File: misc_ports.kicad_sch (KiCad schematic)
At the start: 0 parts

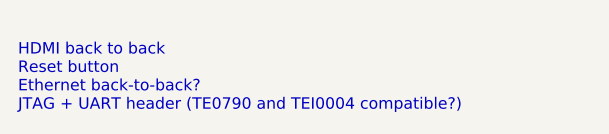
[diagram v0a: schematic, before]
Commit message: add reset button
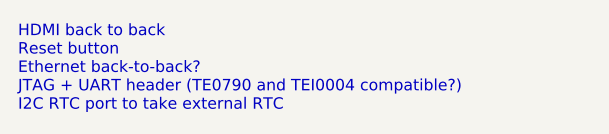
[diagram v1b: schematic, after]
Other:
- note added: "HDMI back to back Reset button Ethernet back-to-back? JTAG + UART header (TE0790 and TEI0004 compatible?) I2C RTC port to take external RTC"
- note removed: "HDMI back to back Reset button Ethernet back-to-back? JTAG + UART header (TE0790 and TEI0004 compatible?)"
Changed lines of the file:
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@@
 (kicad_sch (version 20211123) (generator eeschema)
   (paper "A4")
-  (text "HDMI back to back\nReset button\nEthernet back-to-back?\nJTAG + UART header (TE0790 and TEI0004 compatible?)"
+  (text "HDMI back to back\nReset button\nEthernet back-to-back?\nJTAG + UART header (TE0790 and TEI0004 compatible?)\nI2C RTC port to take external RTC"
     (at 129.54 95.25 0)
     (effects (font (size 1.27 1.27)) (justify left bottom))

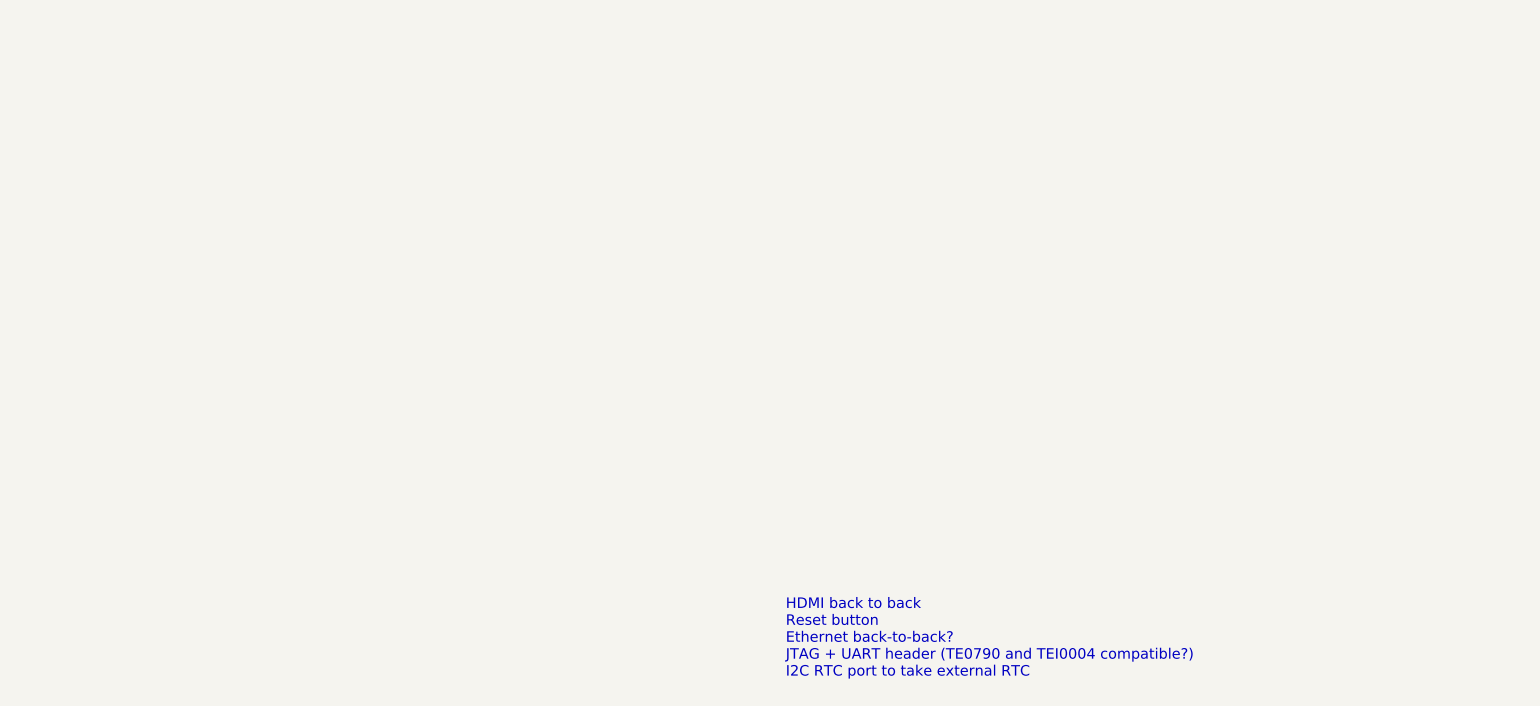
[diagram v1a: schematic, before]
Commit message: add digital video connectors and JTAG/UART header
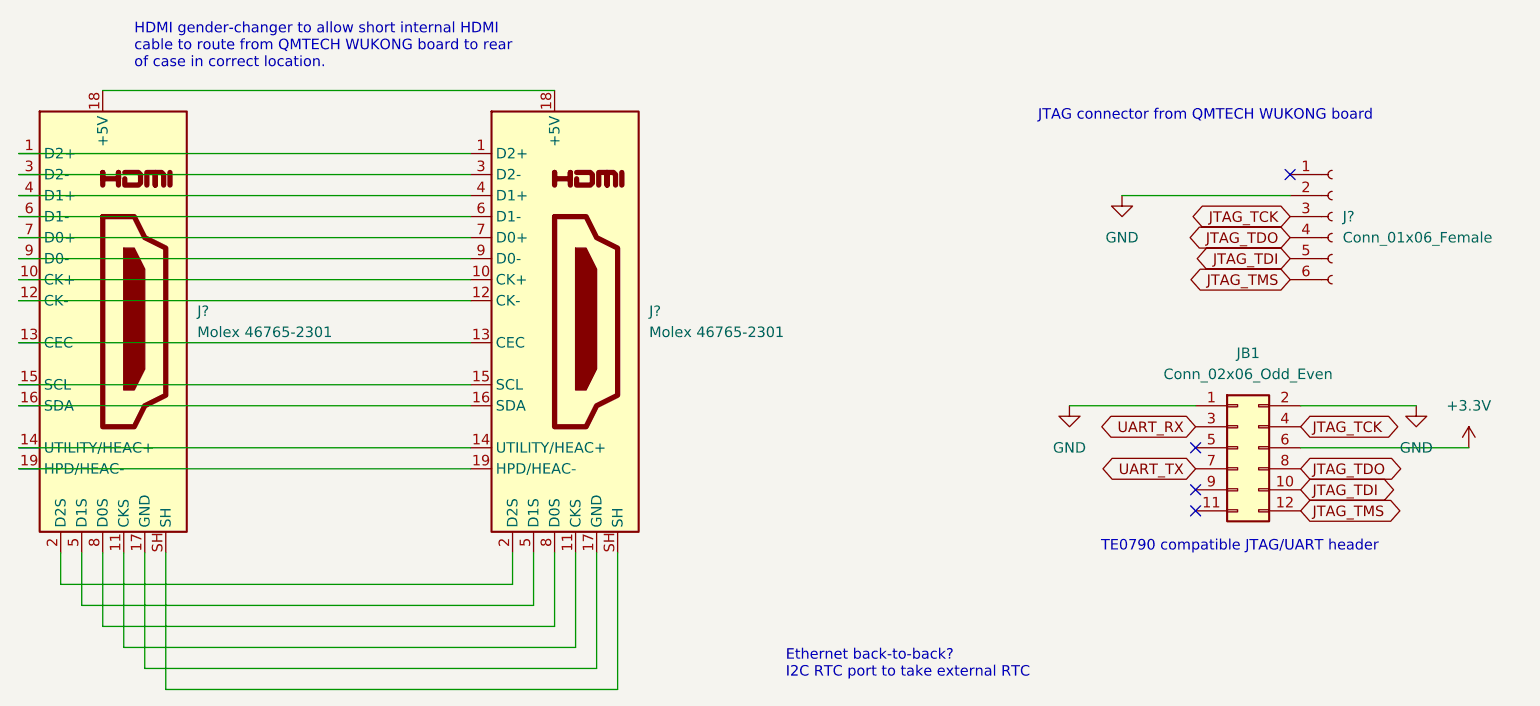
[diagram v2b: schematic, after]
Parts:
- added J? (x2): Molex 46765-2301, Connector_HDMI:HDMI_Micro-D_Molex_46765-2x0x, symbol Connector:HDMI_A_1.4
- added J?: Conn_01x06_Female, Connector_PinSocket_2.54mm:PinSocket_1x06_P2.54mm_Vertical, symbol Connector:Conn_01x06_Female
- added JB1: Conn_02x06_Odd_Even, Connector_PinHeader_2.54mm:PinHeader_2x06_P2.54mm_Vertical, symbol Connector_Generic:Conn_02x06_Odd_Even
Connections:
- new net: J?.1 (D2+), J?.1 (D2+)
- new net: J?.10 (CK+), J?.10 (CK+)
- new net: J?.11 (CKS), J?.11 (CKS)
- new net: J?.12 (CK-), J?.12 (CK-)
- new net: J?.13 (CEC), J?.13 (CEC)
- new net: J?.14 (UTILITY/HEAC+), J?.14 (UTILITY/HEAC+)
- new net: J?.15 (SCL), J?.15 (SCL)
- new net: J?.16 (SDA), J?.16 (SDA)
- new net: J?.17 (GND), J?.17 (GND)
- new net: J?.18 (+5V), J?.18 (+5V)
- new net: J?.19 (HPD/HEAC-), J?.19 (HPD/HEAC-)
- new net: J?.2 (D2S), J?.2 (D2S)
- new net: J?.3 (D2-), J?.3 (D2-)
- new net: J?.4 (D1+), J?.4 (D1+)
- new net: J?.5 (D1S), J?.5 (D1S)
- new net: J?.6 (D1-), J?.6 (D1-)
- new net: J?.7 (D0+), J?.7 (D0+)
- new net: J?.8 (D0S), J?.8 (D0S)
- new net: J?.9 (D0-), J?.9 (D0-)
- new net: J?.SH, J?.SH
- new net +3V3: JB1.6 (Pin_6)
- new net GND: J?.2 (Pin_2), JB1.1 (Pin_1), JB1.2 (Pin_2)
- new net JTAG_TCK: J?.3 (Pin_3), JB1.4 (Pin_4)
- new net JTAG_TDI: J?.5 (Pin_5), JB1.10 (Pin_10)
- new net JTAG_TDO: J?.4 (Pin_4), JB1.8 (Pin_8)
- new net JTAG_TMS: J?.6 (Pin_6), JB1.12 (Pin_12)
- new net UART_RX: JB1.3 (Pin_3)
- new net UART_TX: JB1.7 (Pin_7)
- no-connect marks 0 -> 4
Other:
- note added: "Ethernet back-to-back? I2C RTC port to take external RTC"
- note added: "HDMI gender-changer to allow short internal HDMI cable to route from QMTECH WUKONG board to rear of case in correct location."
- note added: "JTAG connector from QMTECH WUKONG board"
- note added: "TE0790 compatible JTAG/UART header"
- note removed: "HDMI back to back Reset button Ethernet back-to-back? JTAG + UART header (TE0790 and TEI0004 compatible?) I2C RTC port to take external RTC"

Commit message: add notes for other ports
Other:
- note added: "Ethernet back-to-back? I2C RTC port to take external RTC microSD, because early WUKONG boards lack SD card"
- note removed: "Ethernet back-to-back? I2C RTC port to take external RTC"
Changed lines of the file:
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@@
     (effects (font (size 1.27 1.27)) (justify left bottom))
   )
-  (text "Ethernet back-to-back?\nI2C RTC port to take external RTC"
+  (text "Ethernet back-to-back?\nI2C RTC port to take external RTC\nmicroSD, because early WUKONG boards lack SD card"
     (at 129.54 95.25 0)
     (effects (font (size 1.27 1.27)) (justify left bottom))

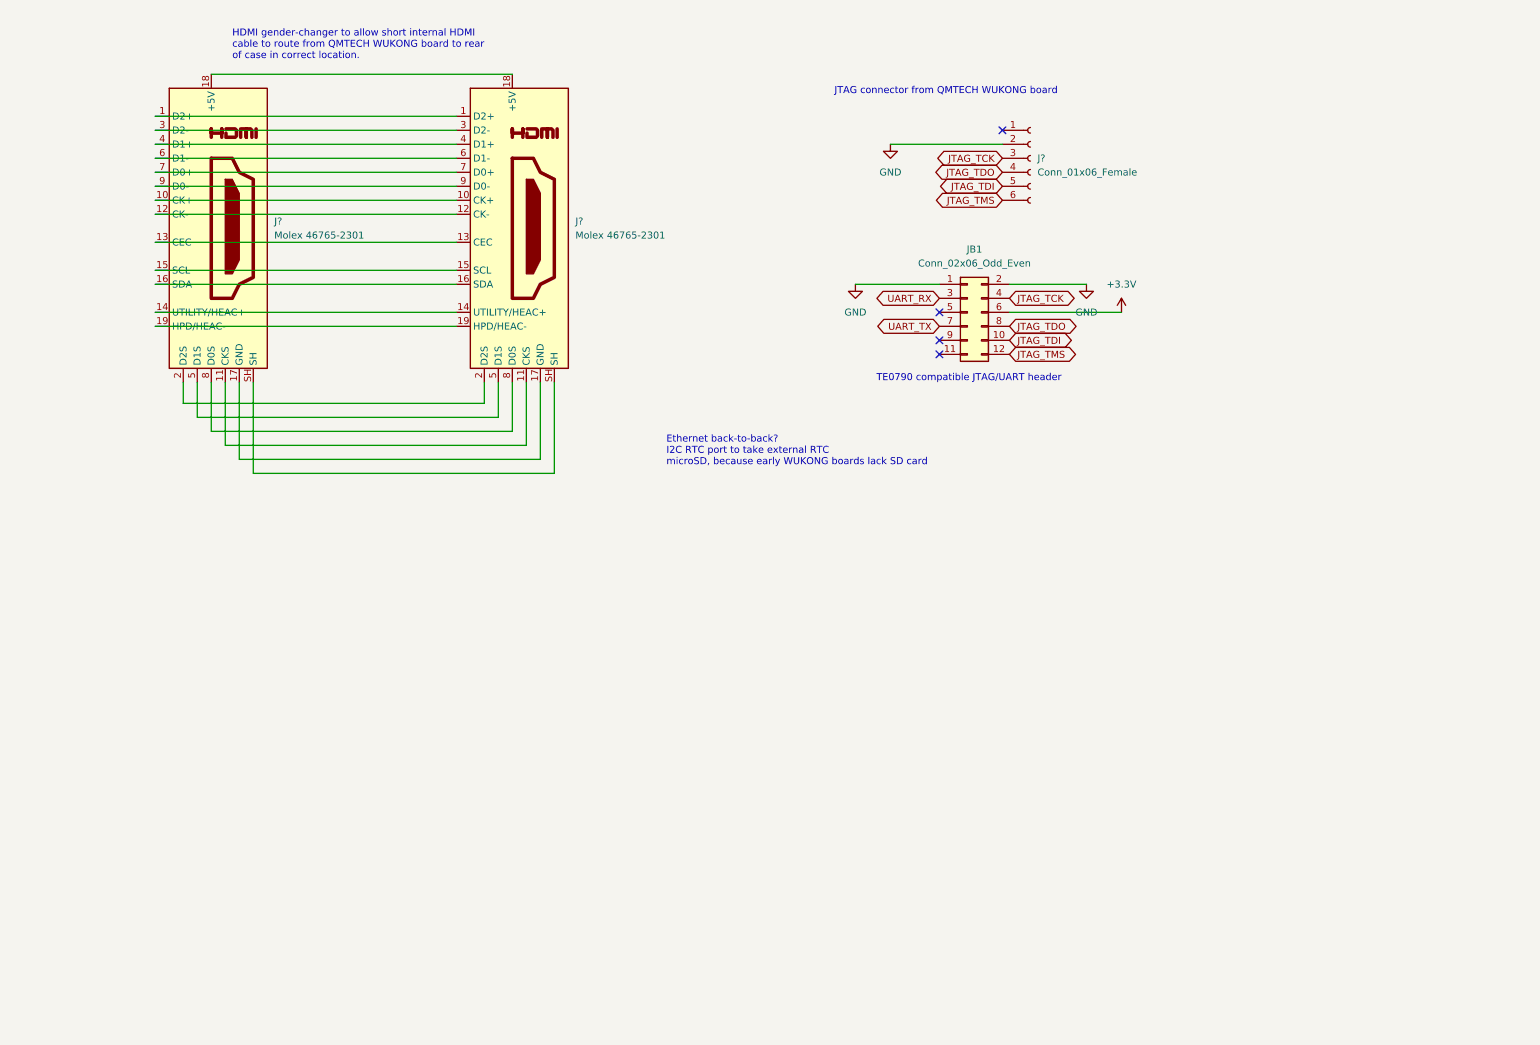
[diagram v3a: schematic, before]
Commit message: add 8-way dipswitch bank
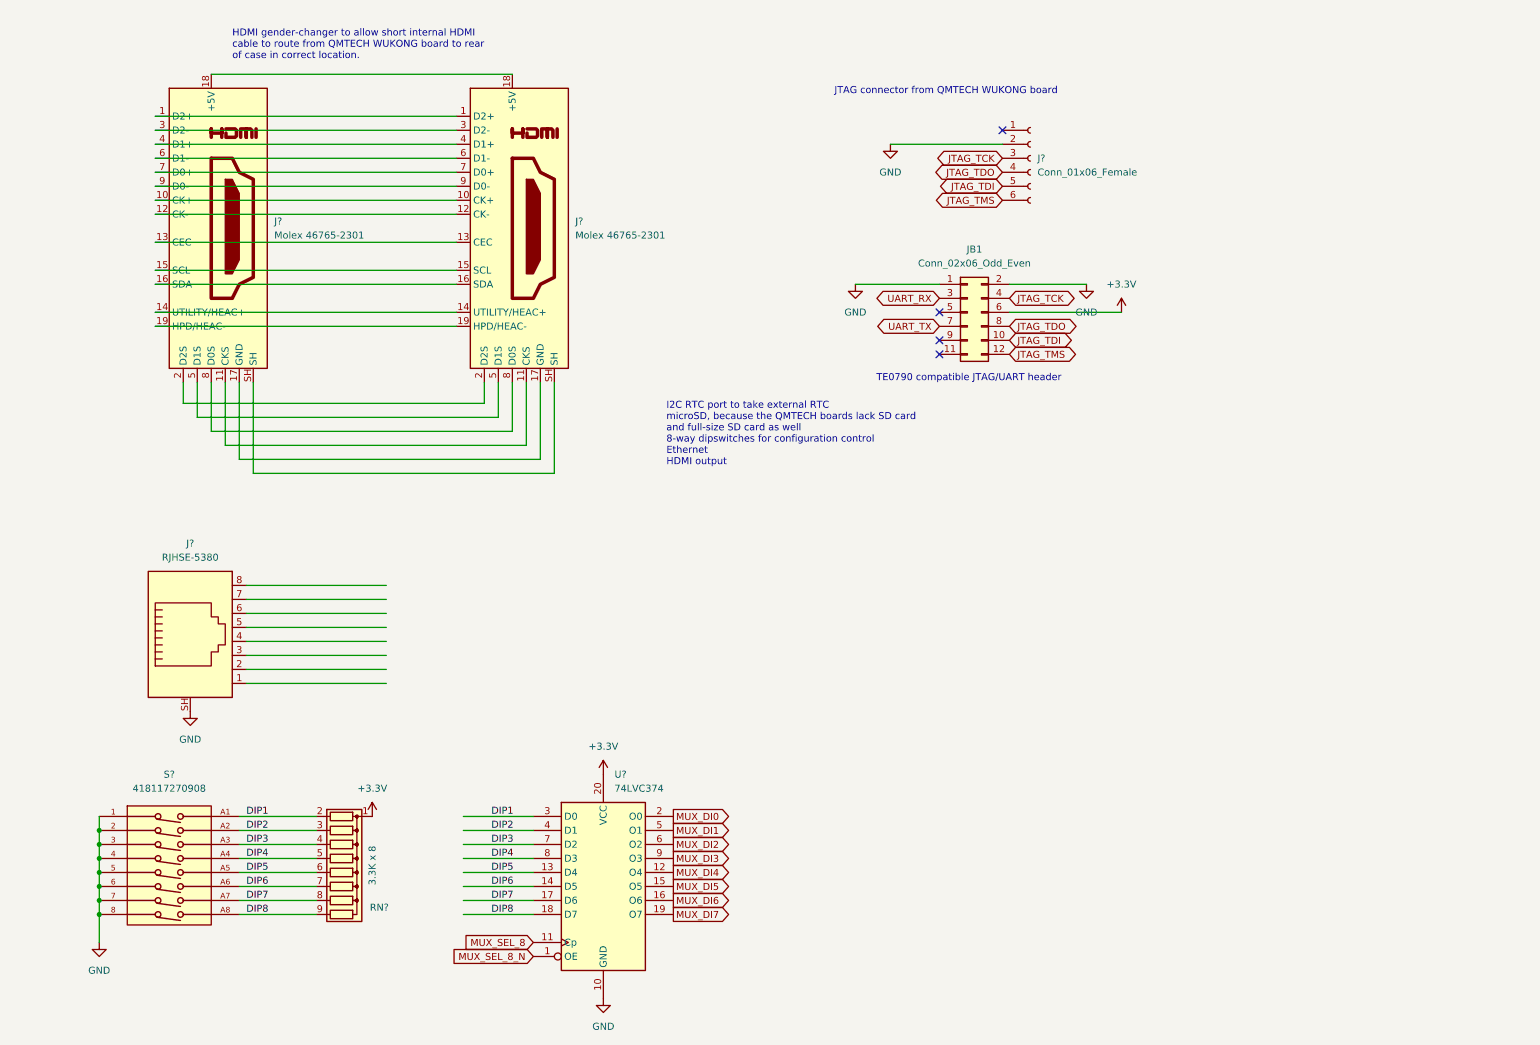
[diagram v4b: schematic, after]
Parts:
- added J?: RJHSE-5380, Connector_RJ:RJ45_Amphenol_RJHSE5380, symbol Connector:RJ45_Shielded
- added RN?: 3.3K x 8, Resistor_THT:R_Array_SIP9, symbol Device:R_Network08
- added S?: 418117270908, snapeda:418117270908, symbol 00Project-DIP-Switch:418117270908
- added U?: 74LVC374, Package_DIP:DIP-20_W7.62mm, symbol 74xx:74HC374
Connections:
- net +3V3: now also RN?.1 (common), U?.20 (VCC)
- net GND: now also J?.SH, S?.1, S?.2, S?.3, S?.4, S?.5, S?.6, S?.7, S?.8, U?.10 (GND)
- new net DIP1: RN?.2 (R1), S?.A1, U?.3 (D0)
- new net DIP2: RN?.3 (R2), S?.A2, U?.4 (D1)
- new net DIP3: RN?.4 (R3), S?.A3, U?.7 (D2)
- new net DIP4: RN?.5 (R4), S?.A4, U?.8 (D3)
- new net DIP5: RN?.6 (R5), S?.A5, U?.13 (D4)
- new net DIP6: RN?.7 (R6), S?.A6, U?.14 (D5)
- new net DIP7: RN?.8 (R7), S?.A7, U?.17 (D6)
- new net DIP8: RN?.9 (R8), S?.A8, U?.18 (D7)
- new net MUX_DI0: U?.2 (O0)
- new net MUX_DI1: U?.5 (O1)
- new net MUX_DI2: U?.6 (O2)
- new net MUX_DI3: U?.9 (O3)
- new net MUX_DI4: U?.12 (O4)
- new net MUX_DI5: U?.15 (O5)
- new net MUX_DI6: U?.16 (O6)
- new net MUX_DI7: U?.19 (O7)
- new net MUX_SEL_8: U?.11 (Cp)
- new net MUX_SEL_8_N: U?.1 (OE)
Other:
- note added: "I2C RTC port to take external RTC microSD, because the QMTECH boards lack SD card and full-size SD card as well 8-way dipswitches for configuration control Ethernet HDMI output"
- note removed: "Ethernet back-to-back? I2C RTC port to take external RTC microSD, because early WUKONG boards lack SD card"

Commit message: work on ethernet
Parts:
- removed J?: RJHSE-5380, Connector_RJ:RJ45_Amphenol_RJHSE5380, symbol Connector:RJ45_Shielded
- added J?: Wuerth_7499010121A, Connector_RJ:RJ45_Wuerth_7499010121A_Horizontal, symbol Connector:Wuerth_7499010121A
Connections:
- net GND: now also J?.SH
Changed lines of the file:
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@@
-    (stroke (width 0) (type default) (color 0 0 0 0))
-  )
-  (wire (pts (xy 53.34 124.46) (xy 78.74 124.46))
     (stroke (width 0) (type default) (color 0 0 0 0))
   )
@@
     (pin "1")
   )
-  (symbol (lib_id "Connector:RJ45_Shielded") (at 43.18 127 0) (unit 1)
-    (in_bom yes) (on_board yes) (fields_autoplaced)
-    (property "Reference" "J?" (id 0) (at 43.18 109.22 0))
-    (property "Value" "RJHSE-5380" (id 1) (at 43.18 111.76 0))
-    (property "Footprint" "Connector_RJ:RJ45_Amphenol_RJHSE5380" (id 2) (at 43.18 126.365 90)
-      (effects (font (size 1.27 1.27)) hide)
-    )
-    (property "Datasheet" "~" (id 3) (at 43.18 126.365 90)
-      (effects (font (size 1.27 1.27)) hide)
-    )
-    (pin "1")
-    (pin "2")
-    (pin "3")
-    (pin "4")
-    (pin "5")
-    (pin "6")
-    (pin "7")
-    (pin "8")
-    (pin "SH")
-  )
   (symbol (lib_id "Connector_Generic:Conn_02x06_Odd_Even") (at 184.15 67.31 0) (unit 1)
     (in_bom yes) (on_board yes) (fields_autoplaced)
@@
     (pin "6")
   )
-  (symbol (lib_id "power:GND") (at 43.18 139.7 0) (unit 1)
-    (in_bom yes) (on_board yes) (fields_autoplaced)
-    (property "Reference" "#PWR?" (id 0) (at 43.18 146.05 0)
-      (effects (font (size 1.27 1.27)) hide)
-    )
-    (property "Value" "GND" (id 1) (at 43.18 144.78 0))
-    (property "Footprint" "" (id 2) (at 43.18 139.7 0)
-      (effects (font (size 1.27 1.27)) hide)
-    )
-    (property "Datasheet" "" (id 3) (at 43.18 139.7 0)
+  (symbol (lib_id "power:GND") (at 38.1 139.7 0) (unit 1)
+    (in_bom yes) (on_board yes) (fields_autoplaced)
+    (property "Reference" "#PWR?" (id 0) (at 38.1 146.05 0)
+      (effects (font (size 1.27 1.27)) hide)
+    )
+    (property "Value" "GND" (id 1) (at 38.1 144.78 0))
+    (property "Footprint" "" (id 2) (at 38.1 139.7 0)
+      (effects (font (size 1.27 1.27)) hide)
+    )
+    (property "Datasheet" "" (id 3) (at 38.1 139.7 0)
       (effects (font (size 1.27 1.27)) hide)
     )
@@
     (pin "1")
   )
+  (symbol (lib_id "Connector:Wuerth_7499010121A") (at 38.1 124.46 0) (unit 1)
+    (in_bom yes) (on_board yes)
+    (property "Reference" "J?" (id 0) (at 24.13 123.1899 0)
+      (effects (font (size 1.27 1.27)) (justify right))
+    )
+    (property "Value" "Wuerth_7499010121A" (id 1) (at 20.32 114.3 90)
+      (effects (font (size 1.27 1.27)) (justify right))
+    )
+    (property "Footprint" "Connector_RJ:RJ45_Wuerth_7499010121A_Horizontal" (id 2) (at 38.1 143.51 0)
+      (effects (font (size 1.27 1.27)) hide)
+    )
+    (property "Datasheet" "http://katalog.we-online.de/pbs/datasheet/7499010121A.pdf" (id 3) (at 27.559 130.429 0)
+      (effects (font (size 1.27 1.27)) (justify left top) hide)
+    )
+    (pin "1")
+    (pin "10")
+    (pin "11")
+    (pin "12")
+    (pin "2")
+    (pin "3")
+    (pin "4")
+    (pin "5")
+    (pin "6")
+    (pin "8")
+    (pin "9")
+    (pin "SH")
+  )
   (symbol (lib_id "power:GND") (at 163.83 62.23 0) (unit 1)

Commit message: add footprint for ferrite bead, work on eth phy
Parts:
- removed J?: Molex 46765-2301, Connector_HDMI:HDMI_Micro-D_Molex_46765-2x0x, symbol Connector:HDMI_A_1.4
- added C? (x4): C, symbol Device:C
- added FB?: FerriteBead FT-3AMB4ARLY-PF, snapeda:Ferrite_Bead_Axial_L10.0mm_D4.5mm_P15.00mm_Horizontal, symbol Device:FerriteBead
- added U?: DP83826, Package_DFN_QFN:QFN-32-1EP_5x5mm_P0.5mm_EP3.3x3.3mm_ThermalVias, symbol 00Project-Eth-Phy:DP83826
- JB1: value Conn_02x06_Odd_Even -> TE0790-03
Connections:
- net +3V3: now also FB?.1
- net GND: now also C?.2, C?.2, C?.2, C?.2, U?.1 (ENHANCED/~{BASIC}), U?.33 (GND/Thermal_Pad)
- new net: C?.1, C?.1, C?.1, C?.1, FB?.2, U?.17 (VDDIO), U?.3 (VDDA3V3)
- new net ETH_MDC: U?.12 (MDC)
- new net ETH_MDIO: U?.11 (MDIO)
- new net ETH_RESET: U?.32 (~{RST})
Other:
- note added: "JTAG connector from QMTECH Kintex325 board"
- note removed: "HDMI gender-changer to allow short internal HDMI cable to route from QMTECH WUKONG board to rear of case in correct location."
- note removed: "JTAG connector from QMTECH WUKONG board"
- moved on the sheet: J?, JB1, RN?, S?, U?
